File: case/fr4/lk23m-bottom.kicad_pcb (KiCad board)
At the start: 2 copper layers, 76.2 x 119.1 mm, 10 parts

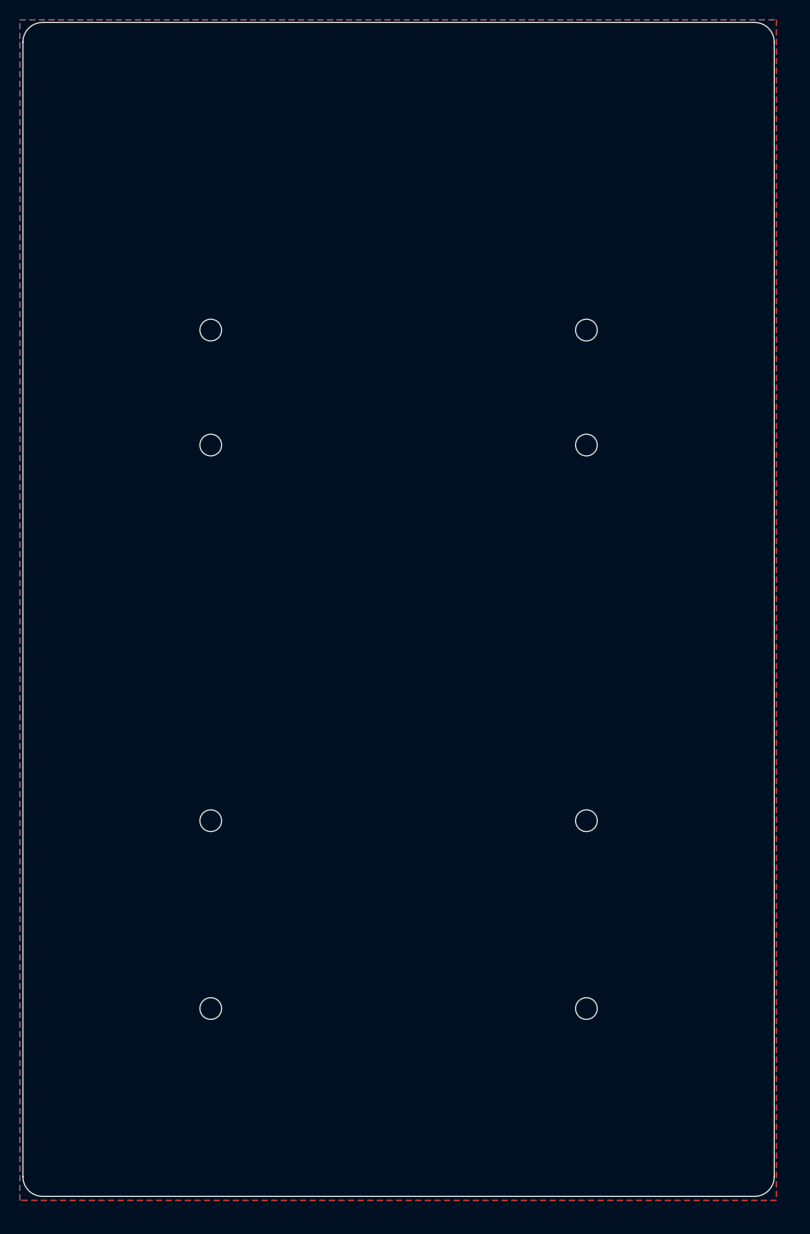
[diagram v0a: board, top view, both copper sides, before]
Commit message: Fix reset switch position in FR4 case
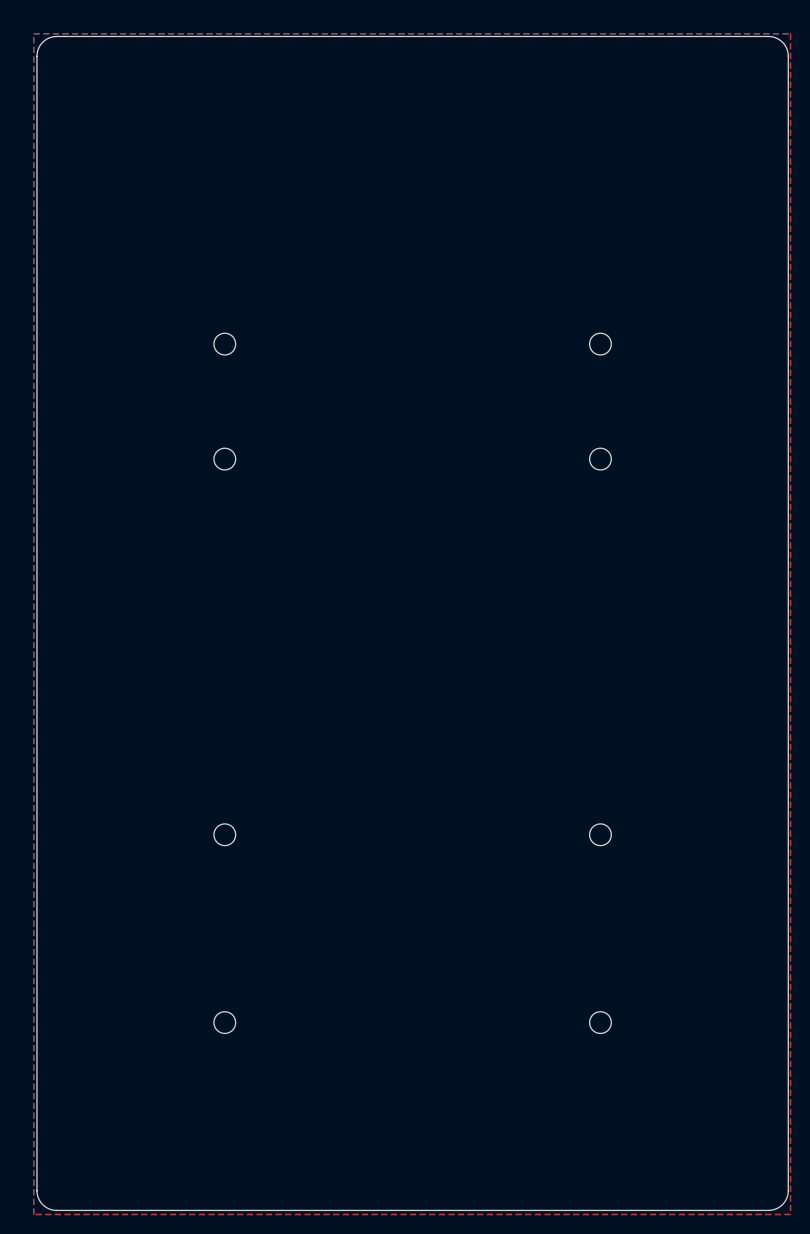
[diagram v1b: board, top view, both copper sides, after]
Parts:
- moved H9 2.12 mm to (62.3, 51.4)
- moved H4 2.02 mm to (87.2, 111.0)
- moved H5 2.02 mm to (87.2, 61.2)
- moved H2 2.02 mm to (87.2, 72.9)
- moved H8 2.02 mm to (49.0, 111.0)
- moved H1 2.02 mm to (49.0, 61.2)
- moved H6 2.02 mm to (49.0, 72.9)
- moved H7 2.02 mm to (87.2, 130.0)
- moved H3 2.02 mm to (49.0, 130.0)
- moved H10 1.91 mm to (73.9, 51.4)
